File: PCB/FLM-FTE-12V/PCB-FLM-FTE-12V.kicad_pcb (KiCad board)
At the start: 2 copper layers, 120 x 75 mm, 54 parts, among them CN1 AKZ700-2-5,08V, CN2 AKZ700-2-5,08V, J1 BPSC-4, J2 MCS-6, J3 BPSC-2, Q1 TIP120, Q2 BC547, Q3 BC547, Q4 BC547, U1 ESP32-WROOM-32E-N8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

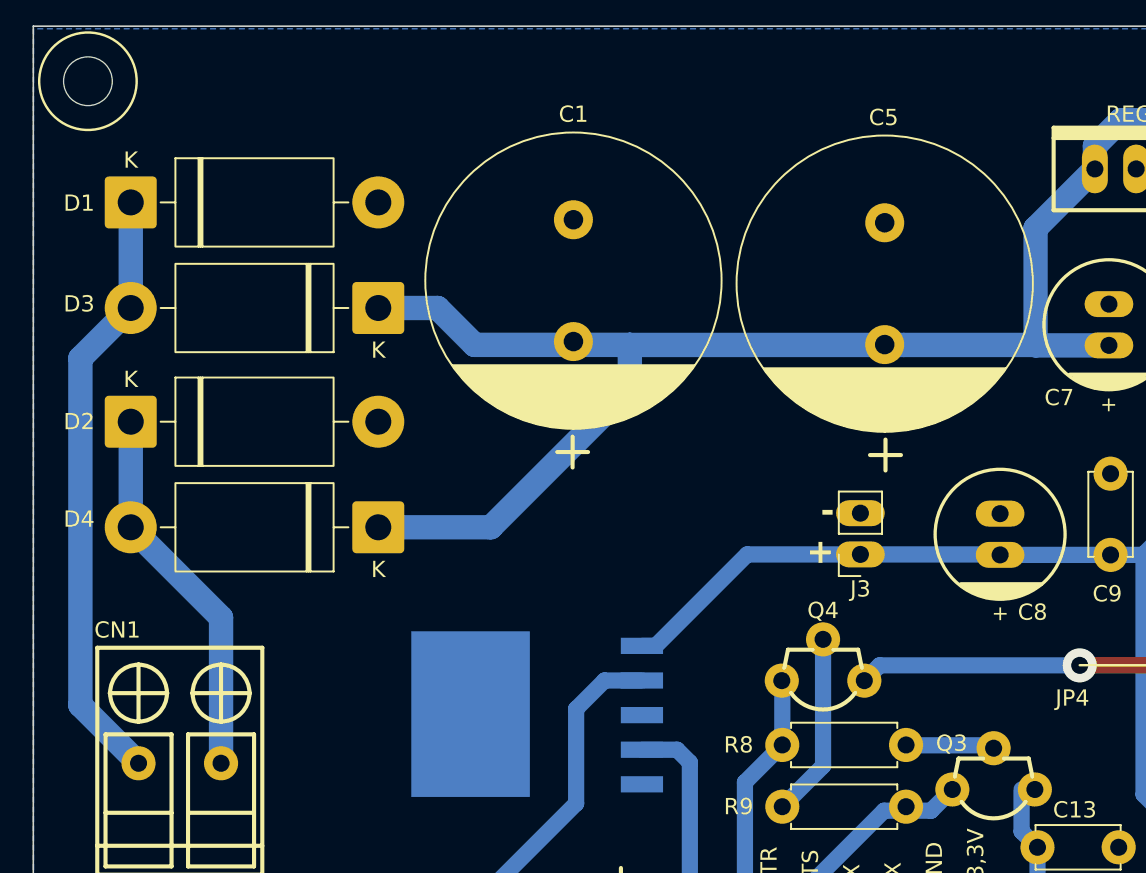
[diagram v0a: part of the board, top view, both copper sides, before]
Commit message: Substituição do C1 e C5
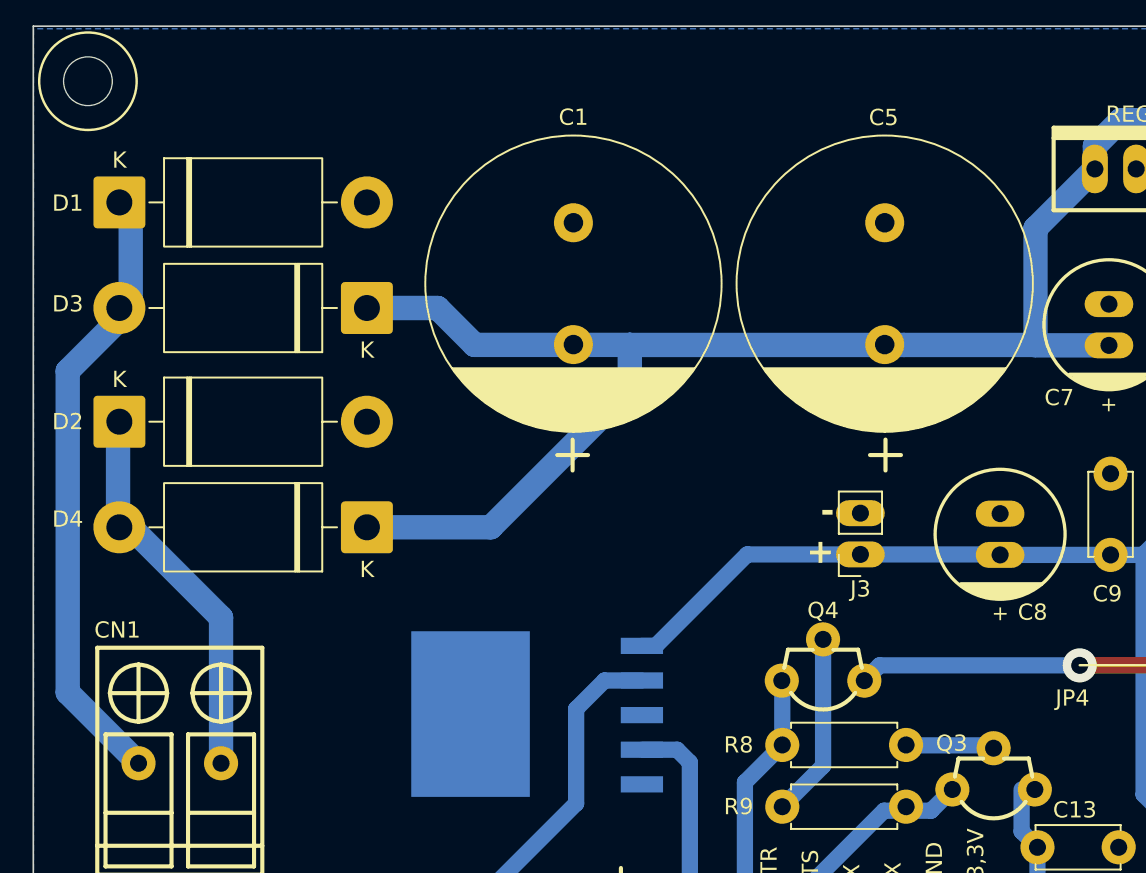
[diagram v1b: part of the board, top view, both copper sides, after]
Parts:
- moved D1 0.70 mm to (52.0, 44.4)
- moved D2 0.70 mm to (52.0, 57.9)
- moved D3 0.70 mm to (67.2, 50.9)
- moved D4 0.70 mm to (67.2, 64.4)
- moved C1 0.19 mm to (80.0, 53.2)
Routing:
- net Net-(D2-K): track 23.3 -> 24.8 mm
- net +15V: track 113.6 -> 115.0 mm
- net Net-(D1-K): track 37.3 -> 37.9 mm
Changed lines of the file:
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@@
 	(footprint "Diode_THT:D_DO-201AD_P15.24mm_Horizontal"
 		(layer "F.Cu")
-		(at 67.945 64.435 180)
+		(at 67.245 64.435 180)
 		(descr "Diode, DO-201AD series, Axial, Horizontal, pin pitch=15.24mm, length*diameter=9.5*5.2mm^2, http://www.diodes.com/_files/packages/DO-201AD.pdf")
 		(tags "Diode DO-201AD series Axial Horizontal pin pitch 15.24mm  length 9.5mm diameter 5.2mm")
@@
 	(footprint "Capacitor_THT:CP_Radial_D18.0mm_P7.50mm"
 		(layer "F.Cu")
-		(at 79.95854 53.001151 90)
+		(at 79.95854 53.187134 90)
 		(descr "CP, Radial series, Radial, pin pitch=7.50mm, diameter=18mm, height=35mm, Electrolytic Capacitor")
 		(tags "CP Radial series Radial pin pitch 7.50mm diameter 18mm height 35mm Electrolytic Capacitor")
@@
 	(footprint "Diode_THT:D_DO-201AD_P15.24mm_Horizontal"
 		(layer "F.Cu")
-		(at 52.705 44.435)
+		(at 52.005 44.435)
 		(descr "Diode, DO-201AD series, Axial, Horizontal, pin pitch=15.24mm, length*diameter=9.5*5.2mm^2, http://www.diodes.com/_files/packages/DO-201AD.pdf")
 		(tags "Diode DO-201AD series Axial Horizontal pin pitch 15.24mm  length 9.5mm diameter 5.2mm")
@@
 	(footprint "Diode_THT:D_DO-201AD_P15.24mm_Horizontal"
 		(layer "F.Cu")
-		(at 67.945 50.935 180)
+		(at 67.245 50.935 180)
 		(descr "Diode, DO-201AD series, Axial, Horizontal, pin pitch=15.24mm, length*diameter=9.5*5.2mm^2, http://www.diodes.com/_files/packages/DO-201AD.pdf")
 		(tags "Diode DO-201AD series Axial Horizontal pin pitch 15.24mm  length 9.5mm diameter 5.2mm")
@@
 	(footprint "Diode_THT:D_DO-201AD_P15.24mm_Horizontal"
 		(layer "F.Cu")
-		(at 52.705 57.935)
+		(at 52.005 57.935)
 		(descr "Diode, DO-201AD series, Axial, Horizontal, pin pitch=15.24mm, length*diameter=9.5*5.2mm^2, http://www.diodes.com/_files/packages/DO-201AD.pdf")
 		(tags "Diode DO-201AD series Axial Horizontal pin pitch 15.24mm  length 9.5mm diameter 5.2mm")
@@
 	)
 	(segment
-		(start 71.6 50.935)
-		(end 73.87 53.205)
+		(start 67.245 64.435)
+		(end 74.87 64.435)
 		(width 1.5)
 		(layer "B.Cu")
@@
 	)
 	(segment
-		(start 83.43 55.875)
-		(end 83.43 53.21)
+		(start 67.245 50.935)
+		(end 71.6 50.935)
 		(width 1.5)
 		(layer "B.Cu")
@@
 	)
 	(segment
-		(start 67.945 64.435)
-		(end 74.87 64.435)
+		(start 126.29 41.212309)
+		(end 126.29 43.105)
 		(width 1.5)
 		(layer "B.Cu")
@@
 	)
 	(segment
-		(start 126.29 41.212309)
-		(end 126.29 43.105)
+		(start 113.647309 39.375)
+		(end 119.465 39.375)
 		(width 1.5)
 		(layer "B.Cu")
@@
 	)
 	(segment
-		(start 113.647309 39.375)
-		(end 119.465 39.375)
+		(start 83.43 55.875)
+		(end 83.43 53.21)
 		(width 1.5)
 		(layer "B.Cu")
@@
 	)
 	(segment
-		(start 112.06 42.375)
-		(end 112.06 40.962309)
+		(start 73.87 53.205)
+		(end 83.425 53.205)
 		(width 1.5)
 		(layer "B.Cu")
@@
 	)
 	(segment
-		(start 108.43 53.235)
-		(end 108.405 53.21)
+		(start 112.06 42.375)
+		(end 112.06 40.962309)
 		(width 1.5)
 		(layer "B.Cu")
@@
 	)
 	(segment
-		(start 73.87 53.205)
-		(end 83.425 53.205)
-		(width 1.5)
-		(layer "B.Cu")
-		(net "+15V")
-	)
-	(segment
 		(start 124.452691 39.375)
 		(end 126.29 41.212309)
@@
 	)
 	(segment
-		(start 67.945 50.935)
-		(end 71.6 50.935)
+		(start 108.405 46.03)
+		(end 108.405 53.21)
 		(width 1.5)
 		(layer "B.Cu")
@@
 	)
 	(segment
-		(start 108.405 46.03)
-		(end 108.405 53.21)
+		(start 120.625 39.475)
+		(end 120.525 39.375)
 		(width 1.5)
 		(layer "B.Cu")
@@
 	)
 	(segment
-		(start 120.625 39.475)
-		(end 120.525 39.375)
+		(start 71.6 50.935)
+		(end 73.87 53.205)
 		(width 1.5)
 		(layer "B.Cu")
@@
 	)
 	(segment
-		(start 58.265 69.995)
-		(end 52.705 64.435)
+		(start 52.005 57.935)
+		(end 52.005 58.635)
+		(width 1.5)
+		(layer "B.Cu")
+		(net "Net-(D2-K)")
+	)
+	(segment
+		(start 52.005 64.435)
+		(end 51.925 64.355)
 		(width 1.5)
 		(layer "B.Cu")
@@
 	(segment
 		(start 52.705 64.435)
-		(end 52.705 57.935)
+		(end 52.005 64.435)
+		(width 1.5)
+		(layer "B.Cu")
+		(net "Net-(D2-K)")
+	)
+	(segment
+		(start 51.925 58.015)
+		(end 52.005 57.935)
+		(width 1.5)
+		(layer "B.Cu")
+		(net "Net-(D2-K)")
+	)
+	(segment
+		(start 51.925 64.355)
+		(end 51.925 58.015)
+		(width 1.5)
+		(layer "B.Cu")
+		(net "Net-(D2-K)")
+	)
+	(segment
+		(start 58.265 69.995)
+		(end 52.705 64.435)
 		(width 1.5)
 		(layer "B.Cu")
@@
 	)
 	(segment
-		(start 53.185 78.962)
-		(end 49.605 75.382)
+		(start 52.705 50.935)
+		(end 52.705 44.435)
 		(width 1.5)
 		(layer "B.Cu")
@@
 	)
 	(segment
-		(start 52.705 44.435)
-		(end 52.705 50.935)
+		(start 48.825 74.602)
+		(end 48.825 54.815)
 		(width 1.5)
 		(layer "B.Cu")
@@
 	)
 	(segment
-		(start 49.605 75.382)
-		(end 49.605 54.035)
+		(start 48.825 54.815)
+		(end 52.705 50.935)
 		(width 1.5)
 		(layer "B.Cu")
@@
 	)
 	(segment
-		(start 49.605 54.035)
-		(end 52.705 50.935)
+		(start 53.185 78.962)
+		(end 48.825 74.602)
 		(width 1.5)
 		(layer "B.Cu")
